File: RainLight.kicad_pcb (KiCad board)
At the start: 2 copper layers, 86.3 x 113.4 mm, 25 parts, among them J1 DTM04-2P (wire pigtail)

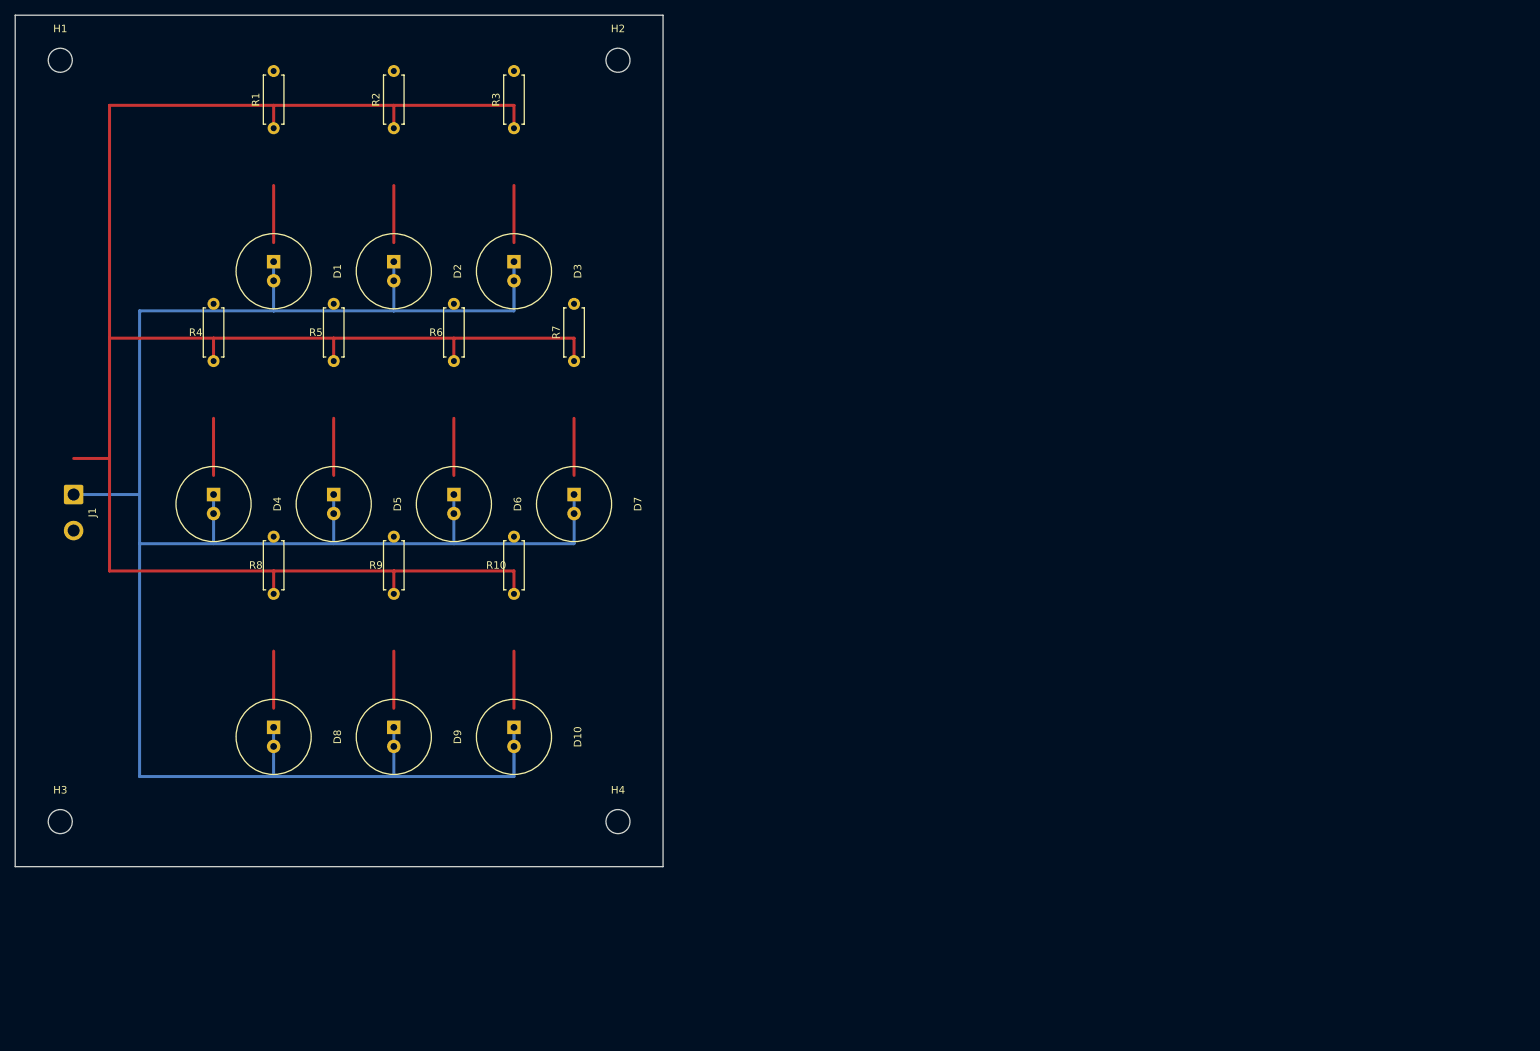
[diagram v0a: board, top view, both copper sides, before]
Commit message: Revert "PCB: redesign for 10mm LEDs (LED_D10.0mm), resize board to 86.3x113.4mm"
This reverts commit 218077b3285cac93fd368fce579aec1e2993a92a.
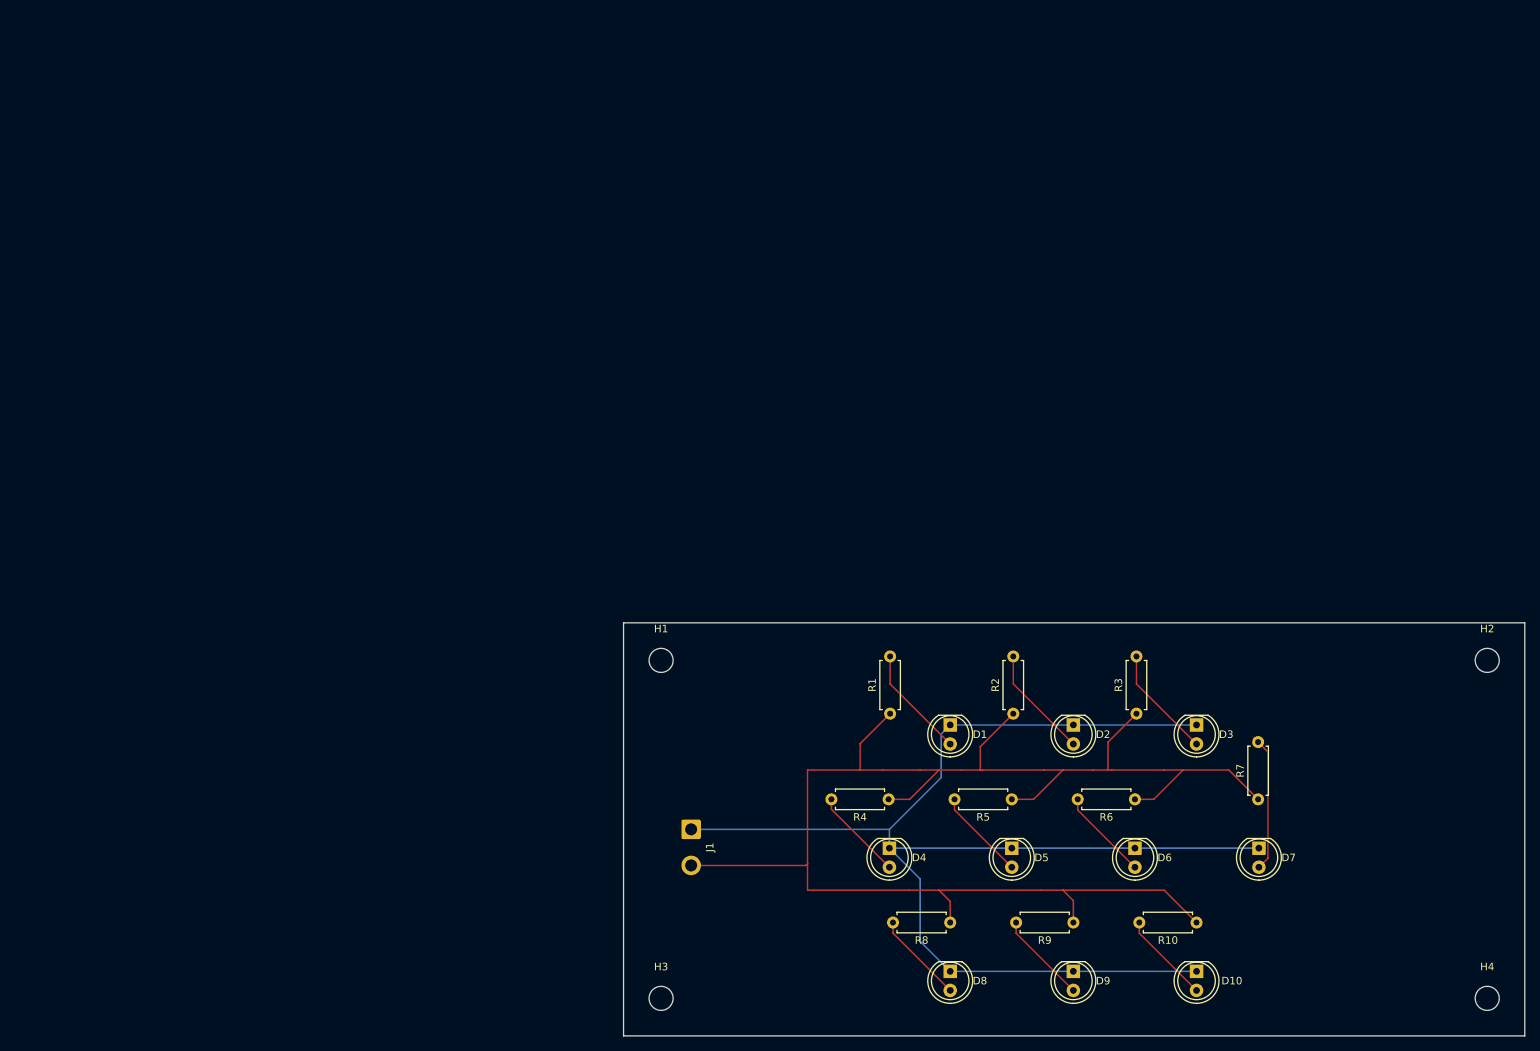
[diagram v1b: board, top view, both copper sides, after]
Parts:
- D1, D10, D2, D3, D4, D5, D6, D7, D8, D9: footprint LED_THT:LED_D10.0mm -> LED_THT:LED_D5.0mm
- H1, H2, H3, H4: footprint MountingHole_3.2mm_M3 -> MountingHole:MountingHole_3.2mm_M3
- moved H2 140.6 mm to (196.0, 85.9)
- moved H4 118.1 mm to (196.0, 130.9)
- moved R3 113.8 mm to (149.3, 93.0)
- moved R2 113.5 mm to (132.9, 93.0)
- moved R1 113.2 mm to (116.5, 93.0)
- moved H1 113.1 mm to (86.0, 85.9)
- moved D3 109.8 mm to (157.3, 94.5)
- moved D2 109.5 mm to (140.9, 94.5)
- moved D1 109.2 mm to (124.5, 94.5)
- moved R7 108.2 mm to (165.5, 104.4)
- moved R6 107.8 mm to (149.1, 104.4), turned to 180 degrees
- moved R5 107.5 mm to (132.7, 104.4), turned to 180 degrees
- moved R4 107.2 mm to (116.3, 104.4), turned to 180 degrees
- moved D7 102.6 mm to (165.6, 110.9)
- moved D6 102.2 mm to (149.1, 110.9)
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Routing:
- net GND: track 293.8 -> 180.7 mm
- net VCC: track 266.8 -> 208.9 mm
- net Net-(D7-A): track 7.61 -> 17.7 mm
- net Net-(D3-A): track 7.61 -> 15.0 mm
- net Net-(D2-A): track 7.61 -> 15.0 mm
- net Net-(D1-A): track 7.61 -> 15.0 mm
- net Net-(D4-A): track 7.61 -> 12.2 mm
- net Net-(D9-A): track 7.61 -> 12.2 mm
- net Net-(D10-A): track 7.61 -> 12.2 mm
- net Net-(D8-A): track 7.61 -> 12.2 mm
- net Net-(D6-A): track 7.61 -> 12.2 mm
- net Net-(D5-A): track 7.61 -> 12.2 mm
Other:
- board size 86.3 x 113.4 mm -> 120 x 55 mm

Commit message: your message here
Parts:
- D1, D10, D2, D3, D4, D5, D6, D7, D8, D9: footprint LED_THT:LED_D5.0mm -> LED_THT:LED_D10.0mm
